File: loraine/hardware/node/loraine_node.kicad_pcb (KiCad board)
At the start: 2 copper layers, 50.8 x 53.3 mm, 43 parts, among them CON1 BARREL_JACK, IC1 ATTINY2313A-S, P1 POWER_THRU, P2 POWER, P3 SOLDER_PAD, P4 ICSP, P5 OUTPUTS, P6 BUS, P7 BUS_THRU, Q1 BD679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

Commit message: Split project into node and uplighter
Node now contains ATTINY, bus controller and most logic and programing

Uplighter board is just three LEDs and their drivers (and sense resistors)

Connection between the two is currently a SIL9 but might be better split into three (or so) connectors so the connectors can stably mount the uplighter board.
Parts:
- removed D1: RED, power_led:power_led
- removed D2: GREEN, power_led:power_led
- removed D3: BLUE, power_led:power_led
- removed R1, R2, R3: 0.47R 0.25W, Resistors_SMD:Resistor_SMD0805_HandSoldering
- removed U3, U4, U5: TL4242, 8-son:8-SON
- added P8: CONN_9, Connect:SIL-9, F.Cu at (76.2, 114.2)
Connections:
- P5 pad 1: +12V -> Net-(P5-Pad1)
- P5 pad 11: +12V -> Net-(P5-Pad1)
- P5 pad 13: +12V -> Net-(P5-Pad1)
- P5 pad 15: +12V -> Net-(P5-Pad1)
- P5 pad 3: +12V -> Net-(P5-Pad1)
- P5 pad 5: +12V -> Net-(P5-Pad1)
- P5 pad 7: +12V -> Net-(P5-Pad1)
- P5 pad 9: +12V -> Net-(P5-Pad1)
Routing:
- net Net-(P5-Pad1): track 0.00 -> 63.3 mm
- net +12V: track 89.8 -> 26.5 mm

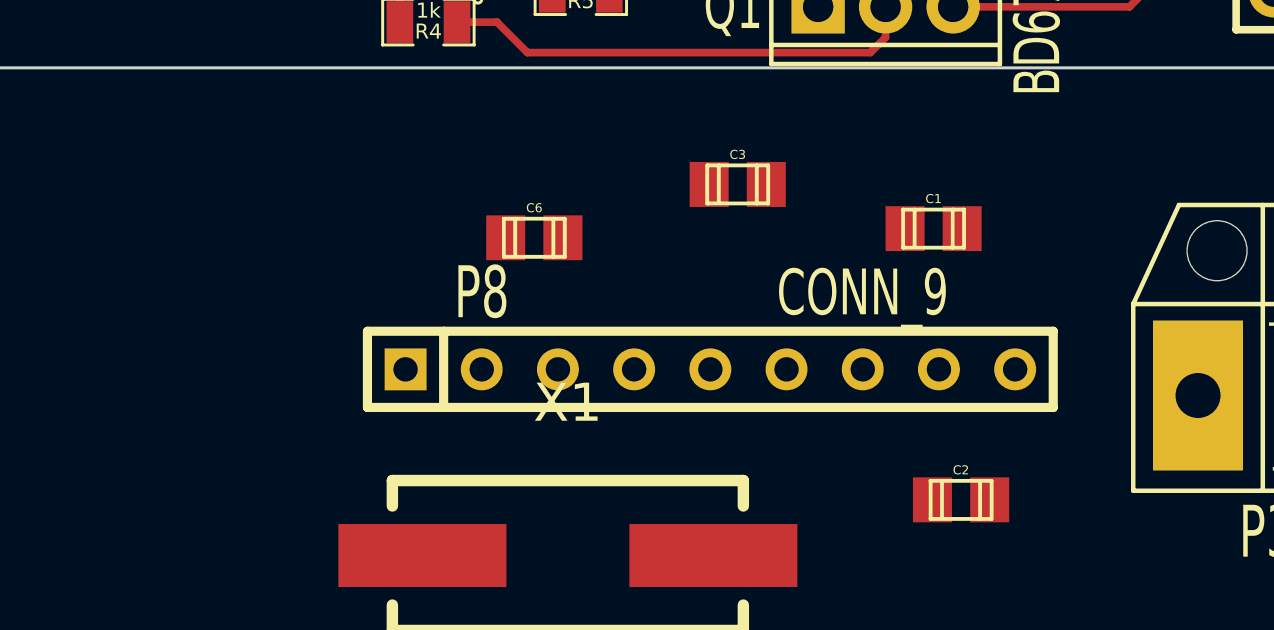
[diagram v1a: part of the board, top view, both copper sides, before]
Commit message: Split board-board connector to 3x SIL3
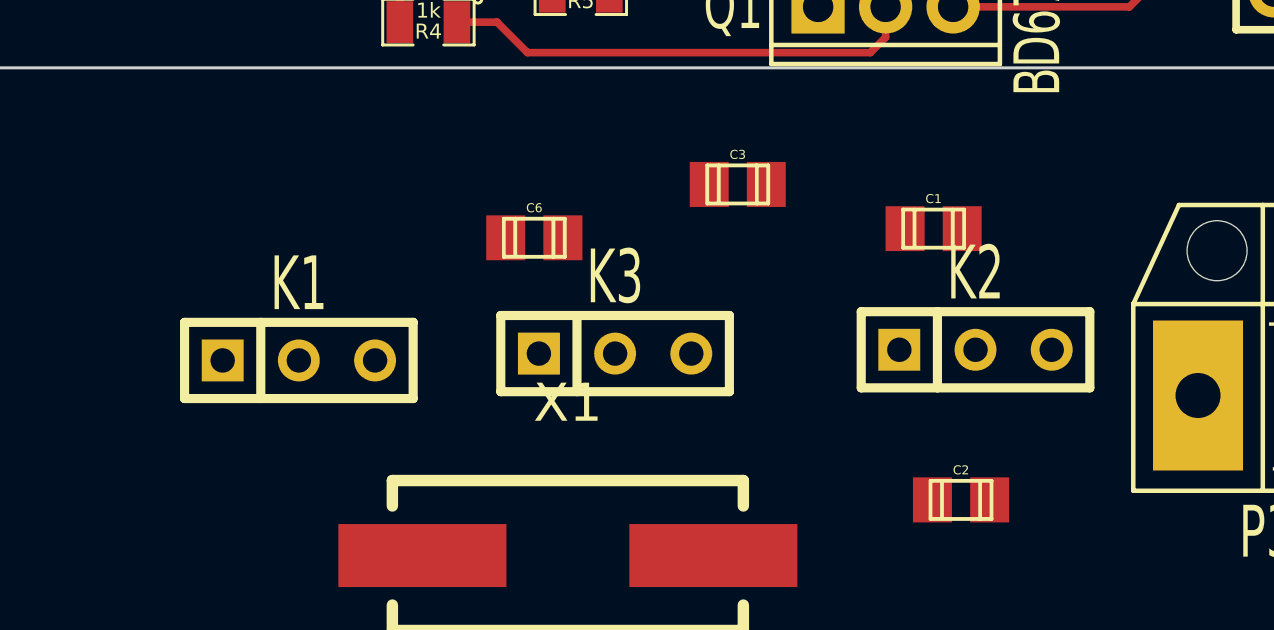
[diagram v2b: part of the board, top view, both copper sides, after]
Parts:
- removed P8: CONN_9, Connect:SIL-9
- added K1: CONN_GND, Connect:SIL-3, F.Cu at (62.5, 113.9)
- added K2: CONN_LEDS, Connect:SIL-3, F.Cu at (85.0, 113.5)
- added K3: CONN_12V, Connect:SIL-3, F.Cu at (73.0, 113.7)
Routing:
- net Net-(P5-Pad1): track 63.3 -> 19.6 mm
- net +12V: track 26.5 -> 70.3 mm
